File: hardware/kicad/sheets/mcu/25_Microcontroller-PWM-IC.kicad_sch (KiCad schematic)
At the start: 16 parts, among them U55 PCA9685PW,118

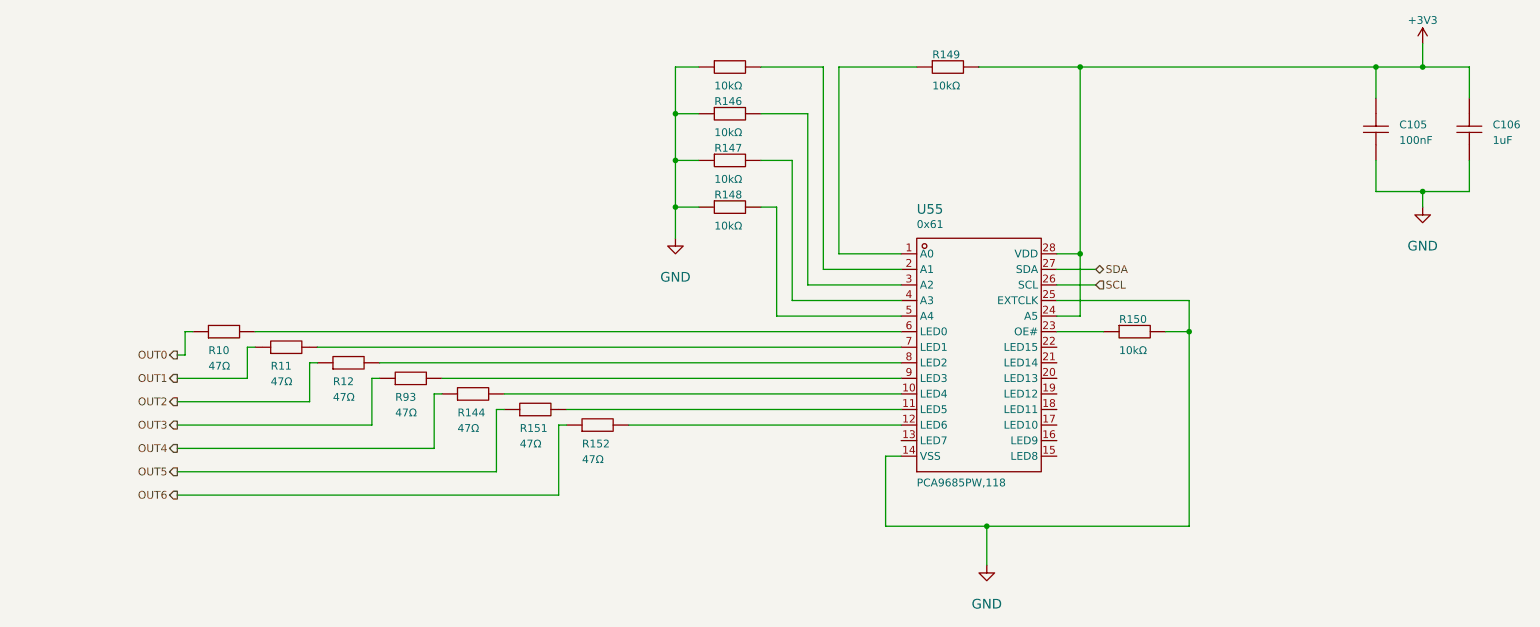
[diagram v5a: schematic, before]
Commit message: current sensing on the servos and cleaning up empty sheets
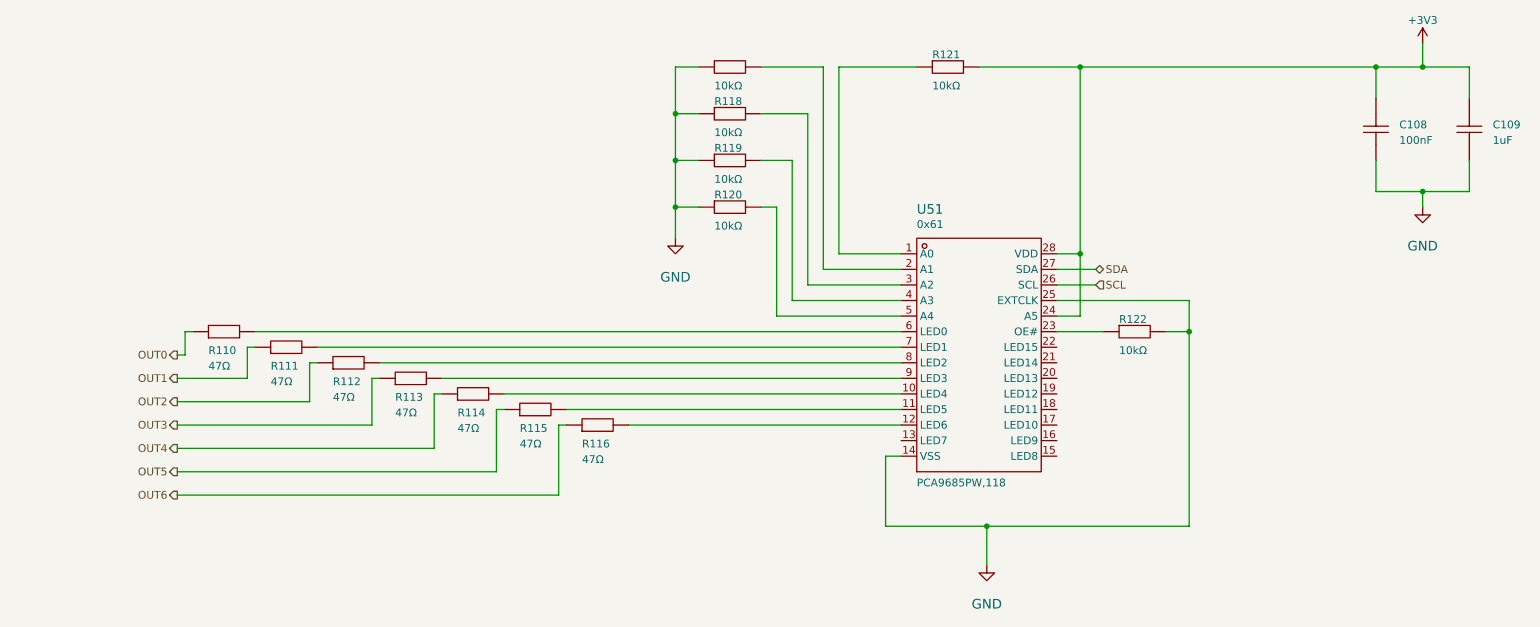
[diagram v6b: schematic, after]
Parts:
- renumbered C105 to C108, C106 to C109, R10 to R110, R11 to R111, R12 to R112, R93 to R113, R144 to R114, R151 to R115, R152 to R116, R145 to R117, R146 to R118, R147 to R119, R148 to R120, R149 to R121, R150 to R122, U55 to U51
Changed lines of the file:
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@@
 		(on_board yes)
 		(dnp no)
-		(property "Reference" "R146"
+		(property "Reference" "R118"
 			(at 128.27 71.12 0)
 			(effects
@@
 			(project "svea_powerboard_rev3"
 				(path "/3f85abf4-0b95-4c4a-b7e9-06f59ca1ea3d/5c2e021f-c2d4-49e2-8c36-9a64f1f12001/8281c4bd-f2fa-451b-b37c-f7eda375ddce"
-					(reference "R146")
+					(reference "R118")
 					(unit 1)
 				)
@@
 		(on_board yes)
 		(dnp no)
-		(property "Reference" "#PWR0175"
+		(property "Reference" "#PWR0158"
 			(at 243.84 60.96 0)
 			(effects
@@
 			(project "svea_powerboard_rev3"
 				(path "/3f85abf4-0b95-4c4a-b7e9-06f59ca1ea3d/5c2e021f-c2d4-49e2-8c36-9a64f1f12001/8281c4bd-f2fa-451b-b37c-f7eda375ddce"
-					(reference "#PWR0175")
+					(reference "#PWR0158")
 					(unit 1)
 				)
@@
 		(on_board yes)
 		(dnp no)
-		(property "Reference" "R10"
+		(property "Reference" "R110"
 			(at 45.72 111.76 0)
 			(effects
@@
 			(project "svea_powerboard_rev3"
 				(path "/3f85abf4-0b95-4c4a-b7e9-06f59ca1ea3d/5c2e021f-c2d4-49e2-8c36-9a64f1f12001/8281c4bd-f2fa-451b-b37c-f7eda375ddce"
-					(reference "R10")
+					(reference "R110")
 					(unit 1)
 				)
@@
 		(on_board yes)
 		(dnp no)
-		(property "Reference" "R144"
+		(property "Reference" "R114"
 			(at 86.36 121.92 0)
 			(effects
@@
 			(project "svea_powerboard_rev3"
 				(path "/3f85abf4-0b95-4c4a-b7e9-06f59ca1ea3d/5c2e021f-c2d4-49e2-8c36-9a64f1f12001/8281c4bd-f2fa-451b-b37c-f7eda375ddce"
-					(reference "R144")
+					(reference "R114")
 					(unit 1)
 				)
@@
 		(on_board yes)
 		(dnp no)
-		(property "Reference" "R150"
+		(property "Reference" "R122"
 			(at 194.31 106.68 0)
 			(effects
@@
 			(project "svea_powerboard_rev3"
 				(path "/3f85abf4-0b95-4c4a-b7e9-06f59ca1ea3d/5c2e021f-c2d4-49e2-8c36-9a64f1f12001/8281c4bd-f2fa-451b-b37c-f7eda375ddce"
-					(reference "R150")
+					(reference "R122")
 					(unit 1)
 				)
@@
 		(on_board yes)
 		(dnp no)
-		(property "Reference" "R11"
+		(property "Reference" "R111"
 			(at 55.88 114.3 0)
 			(effects
@@
 			(project "svea_powerboard_rev3"
 				(path "/3f85abf4-0b95-4c4a-b7e9-06f59ca1ea3d/5c2e021f-c2d4-49e2-8c36-9a64f1f12001/8281c4bd-f2fa-451b-b37c-f7eda375ddce"
-					(reference "R11")
+					(reference "R111")
 					(unit 1)
 				)
@@
 		(on_board yes)
 		(dnp no)
-		(property "Reference" "R12"
+		(property "Reference" "R112"
 			(at 66.04 116.84 0)
 			(effects
@@
 			(project "svea_powerboard_rev3"
 				(path "/3f85abf4-0b95-4c4a-b7e9-06f59ca1ea3d/5c2e021f-c2d4-49e2-8c36-9a64f1f12001/8281c4bd-f2fa-451b-b37c-f7eda375ddce"
-					(reference "R12")
+					(reference "R112")
 					(unit 1)
 				)
@@
 		(on_board yes)
 		(dnp no)
-		(property "Reference" "R93"
+		(property "Reference" "R113"
 			(at 76.2 119.38 0)
 			(effects
@@
 			(project "svea_powerboard_rev3"
 				(path "/3f85abf4-0b95-4c4a-b7e9-06f59ca1ea3d/5c2e021f-c2d4-49e2-8c36-9a64f1f12001/8281c4bd-f2fa-451b-b37c-f7eda375ddce"
-					(reference "R93")
+					(reference "R113")
 					(unit 1)
 				)
@@
 		(on_board yes)
 		(dnp no)
-		(property "Reference" "C106"
+		(property "Reference" "C109"
 			(at 255.27 74.93 90)
 			(effects
@@
 			(project "svea_powerboard_rev3"
 				(path "/3f85abf4-0b95-4c4a-b7e9-06f59ca1ea3d/5c2e021f-c2d4-49e2-8c36-9a64f1f12001/8281c4bd-f2fa-451b-b37c-f7eda375ddce"
-					(reference "C106")
+					(reference "C109")
 					(unit 1)
 				)
@@
 		(on_board yes)
 		(dnp no)
-		(property "Reference" "R149"
+		(property "Reference" "R121"
 			(at 163.83 63.5 0)
 			(effects
@@
 			(project "svea_powerboard_rev3"
 				(path "/3f85abf4-0b95-4c4a-b7e9-06f59ca1ea3d/5c2e021f-c2d4-49e2-8c36-9a64f1f12001/8281c4bd-f2fa-451b-b37c-f7eda375ddce"
-					(reference "R149")
+					(reference "R121")
 					(unit 1)
 				)
@@
 		(on_board yes)
 		(dnp no)
-		(property "Reference" "#PWR0176"
+		(property "Reference" "#PWR0159"
 			(at 243.84 87.63 0)
 			(effects
@@
 			(project "svea_powerboard_rev3"
 				(path "/3f85abf4-0b95-4c4a-b7e9-06f59ca1ea3d/5c2e021f-c2d4-49e2-8c36-9a64f1f12001/8281c4bd-f2fa-451b-b37c-f7eda375ddce"
-					(reference "#PWR0176")
+					(reference "#PWR0159")
 					(unit 1)
 				)
@@
 		(on_board yes)
 		(dnp no)
-		(property "Reference" "#PWR0173"
+		(property "Reference" "#PWR0156"
 			(at 121.92 92.71 0)
 			(effects
@@
 			(project "svea_powerboard_rev3"
 				(path "/3f85abf4-0b95-4c4a-b7e9-06f59ca1ea3d/5c2e021f-c2d4-49e2-8c36-9a64f1f12001/8281c4bd-f2fa-451b-b37c-f7eda375ddce"
-					(reference "#PWR0173")
+					(reference "#PWR0156")
 					(unit 1)
 				)
@@
 		(on_board yes)
 		(dnp no)
-		(property "Reference" "R148"
+		(property "Reference" "R120"
 			(at 128.27 86.36 0)
 			(effects
@@
 			(project "svea_powerboard_rev3"
 				(path "/3f85abf4-0b95-4c4a-b7e9-06f59ca1ea3d/5c2e021f-c2d4-49e2-8c36-9a64f1f12001/8281c4bd-f2fa-451b-b37c-f7eda375ddce"
-					(reference "R148")
+					(reference "R120")
 					(unit 1)
 				)
@@
 		(on_board yes)
 		(dnp no)
-		(property "Reference" "R145"
+		(property "Reference" "R117"
 			(at 128.27 63.5 0)
 			(effects
@@
 			(project "svea_powerboard_rev3"
 				(path "/3f85abf4-0b95-4c4a-b7e9-06f59ca1ea3d/5c2e021f-c2d4-49e2-8c36-9a64f1f12001/8281c4bd-f2fa-451b-b37c-f7eda375ddce"
-					(reference "R145")
+					(reference "R117")
 					(unit 1)
 				)
@@
 		(on_board yes)
 		(dnp no)
-		(property "Reference" "R152"
+		(property "Reference" "R116"
 			(at 106.68 127 0)
 			(effects
@@
 			(project "svea_powerboard_rev3"
 				(path "/3f85abf4-0b95-4c4a-b7e9-06f59ca1ea3d/5c2e021f-c2d4-49e2-8c36-9a64f1f12001/8281c4bd-f2fa-451b-b37c-f7eda375ddce"
-					(reference "R152")
+					(reference "R116")
 					(unit 1)
 				)
@@
 		(on_board yes)
 		(dnp no)
-		(property "Reference" "#PWR0174"
+		(property "Reference" "#PWR0157"
 			(at 172.72 146.05 0)
 			(effects
@@
 			(project "svea_powerboard_rev3"
 				(path "/3f85abf4-0b95-4c4a-b7e9-06f59ca1ea3d/5c2e021f-c2d4-49e2-8c36-9a64f1f12001/8281c4bd-f2fa-451b-b37c-f7eda375ddce"
-					(reference "#PWR0174")
+					(reference "#PWR0157")
 					(unit 1)
 				)
@@
 		(on_board yes)
 		(dnp no)
-		(property "Reference" "C105"
+		(property "Reference" "C108"
 			(at 240.03 74.93 90)
 			(effects
@@
 			(project "svea_powerboard_rev3"
 				(path "/3f85abf4-0b95-4c4a-b7e9-06f59ca1ea3d/5c2e021f-c2d4-49e2-8c36-9a64f1f12001/8281c4bd-f2fa-451b-b37c-f7eda375ddce"
-					(reference "C105")
+					(reference "C108")
 					(unit 1)
 				)
@@
 		(on_board yes)
 		(dnp no)
-		(property "Reference" "U55"
+		(property "Reference" "U51"
 			(at 161.29 88.9 0)
 			(effects
@@
 			(project "svea_powerboard_rev3"
 				(path "/3f85abf4-0b95-4c4a-b7e9-06f59ca1ea3d/5c2e021f-c2d4-49e2-8c36-9a64f1f12001/8281c4bd-f2fa-451b-b37c-f7eda375ddce"
-					(reference "U55")
+					(reference "U51")
 					(unit 1)
 				)
@@
 		(on_board yes)
 		(dnp no)
-		(property "Reference" "R147"
+		(property "Reference" "R119"
 			(at 128.27 78.74 0)
 			(effects
@@
 			(project "svea_powerboard_rev3"
 				(path "/3f85abf4-0b95-4c4a-b7e9-06f59ca1ea3d/5c2e021f-c2d4-49e2-8c36-9a64f1f12001/8281c4bd-f2fa-451b-b37c-f7eda375ddce"
-					(reference "R147")
+					(reference "R119")
 					(unit 1)
 				)
@@
 		(on_board yes)
 		(dnp no)
-		(property "Reference" "R151"
+		(property "Reference" "R115"
 			(at 96.52 124.46 0)
 			(effects
@@
 			(project "svea_powerboard_rev3"
 				(path "/3f85abf4-0b95-4c4a-b7e9-06f59ca1ea3d/5c2e021f-c2d4-49e2-8c36-9a64f1f12001/8281c4bd-f2fa-451b-b37c-f7eda375ddce"
-					(reference "R151")
+					(reference "R115")
 					(unit 1)
 				)

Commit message: new references
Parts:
- renumbered C108 to C123, C109 to C124, R110 to R146, R111 to R147, R112 to R148, R113 to R149, R114 to R150, R115 to R152, R116 to R155, R117 to R157, R118 to R158, R119 to R159, R120 to R160, R121 to R168, R122 to R171, U51 to U59
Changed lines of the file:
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@@
 		(on_board yes)
 		(dnp no)
-		(property "Reference" "R118"
+		(property "Reference" "R158"
 			(at 128.27 71.12 0)
 			(effects
@@
 			(project "svea_powerboard_rev3"
 				(path "/3f85abf4-0b95-4c4a-b7e9-06f59ca1ea3d/5c2e021f-c2d4-49e2-8c36-9a64f1f12001/8281c4bd-f2fa-451b-b37c-f7eda375ddce"
-					(reference "R118")
+					(reference "R158")
 					(unit 1)
 				)
@@
 		(on_board yes)
 		(dnp no)
-		(property "Reference" "#PWR0158"
+		(property "Reference" "#PWR0175"
 			(at 243.84 60.96 0)
 			(effects
@@
 			(project "svea_powerboard_rev3"
 				(path "/3f85abf4-0b95-4c4a-b7e9-06f59ca1ea3d/5c2e021f-c2d4-49e2-8c36-9a64f1f12001/8281c4bd-f2fa-451b-b37c-f7eda375ddce"
-					(reference "#PWR0158")
+					(reference "#PWR0175")
 					(unit 1)
 				)
@@
 		(on_board yes)
 		(dnp no)
-		(property "Reference" "R110"
+		(property "Reference" "R146"
 			(at 45.72 111.76 0)
 			(effects
@@
 			(project "svea_powerboard_rev3"
 				(path "/3f85abf4-0b95-4c4a-b7e9-06f59ca1ea3d/5c2e021f-c2d4-49e2-8c36-9a64f1f12001/8281c4bd-f2fa-451b-b37c-f7eda375ddce"
-					(reference "R110")
+					(reference "R146")
 					(unit 1)
 				)
@@
 		(on_board yes)
 		(dnp no)
-		(property "Reference" "R114"
+		(property "Reference" "R150"
 			(at 86.36 121.92 0)
 			(effects
@@
 			(project "svea_powerboard_rev3"
 				(path "/3f85abf4-0b95-4c4a-b7e9-06f59ca1ea3d/5c2e021f-c2d4-49e2-8c36-9a64f1f12001/8281c4bd-f2fa-451b-b37c-f7eda375ddce"
-					(reference "R114")
+					(reference "R150")
 					(unit 1)
 				)
@@
 		(on_board yes)
 		(dnp no)
-		(property "Reference" "R122"
+		(property "Reference" "R171"
 			(at 194.31 106.68 0)
 			(effects
@@
 			(project "svea_powerboard_rev3"
 				(path "/3f85abf4-0b95-4c4a-b7e9-06f59ca1ea3d/5c2e021f-c2d4-49e2-8c36-9a64f1f12001/8281c4bd-f2fa-451b-b37c-f7eda375ddce"
-					(reference "R122")
+					(reference "R171")
 					(unit 1)
 				)
@@
 		(on_board yes)
 		(dnp no)
-		(property "Reference" "R111"
+		(property "Reference" "R147"
 			(at 55.88 114.3 0)
 			(effects
@@
 			(project "svea_powerboard_rev3"
 				(path "/3f85abf4-0b95-4c4a-b7e9-06f59ca1ea3d/5c2e021f-c2d4-49e2-8c36-9a64f1f12001/8281c4bd-f2fa-451b-b37c-f7eda375ddce"
-					(reference "R111")
+					(reference "R147")
 					(unit 1)
 				)
@@
 		(on_board yes)
 		(dnp no)
-		(property "Reference" "R112"
+		(property "Reference" "R148"
 			(at 66.04 116.84 0)
 			(effects
@@
 			(project "svea_powerboard_rev3"
 				(path "/3f85abf4-0b95-4c4a-b7e9-06f59ca1ea3d/5c2e021f-c2d4-49e2-8c36-9a64f1f12001/8281c4bd-f2fa-451b-b37c-f7eda375ddce"
-					(reference "R112")
+					(reference "R148")
 					(unit 1)
 				)
@@
 		(on_board yes)
 		(dnp no)
-		(property "Reference" "R113"
+		(property "Reference" "R149"
 			(at 76.2 119.38 0)
 			(effects
@@
 			(project "svea_powerboard_rev3"
 				(path "/3f85abf4-0b95-4c4a-b7e9-06f59ca1ea3d/5c2e021f-c2d4-49e2-8c36-9a64f1f12001/8281c4bd-f2fa-451b-b37c-f7eda375ddce"
-					(reference "R113")
+					(reference "R149")
 					(unit 1)
 				)
@@
 		(on_board yes)
 		(dnp no)
-		(property "Reference" "C109"
+		(property "Reference" "C124"
 			(at 255.27 74.93 90)
 			(effects
@@
 			(project "svea_powerboard_rev3"
 				(path "/3f85abf4-0b95-4c4a-b7e9-06f59ca1ea3d/5c2e021f-c2d4-49e2-8c36-9a64f1f12001/8281c4bd-f2fa-451b-b37c-f7eda375ddce"
-					(reference "C109")
+					(reference "C124")
 					(unit 1)
 				)
@@
 		(on_board yes)
 		(dnp no)
-		(property "Reference" "R121"
+		(property "Reference" "R168"
 			(at 163.83 63.5 0)
 			(effects
@@
 			(project "svea_powerboard_rev3"
 				(path "/3f85abf4-0b95-4c4a-b7e9-06f59ca1ea3d/5c2e021f-c2d4-49e2-8c36-9a64f1f12001/8281c4bd-f2fa-451b-b37c-f7eda375ddce"
-					(reference "R121")
+					(reference "R168")
 					(unit 1)
 				)
@@
 		(on_board yes)
 		(dnp no)
-		(property "Reference" "#PWR0159"
+		(property "Reference" "#PWR0176"
 			(at 243.84 87.63 0)
 			(effects
@@
 			(project "svea_powerboard_rev3"
 				(path "/3f85abf4-0b95-4c4a-b7e9-06f59ca1ea3d/5c2e021f-c2d4-49e2-8c36-9a64f1f12001/8281c4bd-f2fa-451b-b37c-f7eda375ddce"
-					(reference "#PWR0159")
+					(reference "#PWR0176")
 					(unit 1)
 				)
@@
 		(on_board yes)
 		(dnp no)
-		(property "Reference" "#PWR0156"
+		(property "Reference" "#PWR0173"
 			(at 121.92 92.71 0)
 			(effects
@@
 			(project "svea_powerboard_rev3"
 				(path "/3f85abf4-0b95-4c4a-b7e9-06f59ca1ea3d/5c2e021f-c2d4-49e2-8c36-9a64f1f12001/8281c4bd-f2fa-451b-b37c-f7eda375ddce"
-					(reference "#PWR0156")
+					(reference "#PWR0173")
 					(unit 1)
 				)
@@
 		(on_board yes)
 		(dnp no)
-		(property "Reference" "R120"
+		(property "Reference" "R160"
 			(at 128.27 86.36 0)
 			(effects
@@
 			(project "svea_powerboard_rev3"
 				(path "/3f85abf4-0b95-4c4a-b7e9-06f59ca1ea3d/5c2e021f-c2d4-49e2-8c36-9a64f1f12001/8281c4bd-f2fa-451b-b37c-f7eda375ddce"
-					(reference "R120")
+					(reference "R160")
 					(unit 1)
 				)
@@
 		(on_board yes)
 		(dnp no)
-		(property "Reference" "R117"
+		(property "Reference" "R157"
 			(at 128.27 63.5 0)
 			(effects
@@
 			(project "svea_powerboard_rev3"
 				(path "/3f85abf4-0b95-4c4a-b7e9-06f59ca1ea3d/5c2e021f-c2d4-49e2-8c36-9a64f1f12001/8281c4bd-f2fa-451b-b37c-f7eda375ddce"
-					(reference "R117")
+					(reference "R157")
 					(unit 1)
 				)
@@
 		(on_board yes)
 		(dnp no)
-		(property "Reference" "R116"
+		(property "Reference" "R155"
 			(at 106.68 127 0)
 			(effects
@@
 			(project "svea_powerboard_rev3"
 				(path "/3f85abf4-0b95-4c4a-b7e9-06f59ca1ea3d/5c2e021f-c2d4-49e2-8c36-9a64f1f12001/8281c4bd-f2fa-451b-b37c-f7eda375ddce"
-					(reference "R116")
+					(reference "R155")
 					(unit 1)
 				)
@@
 		(on_board yes)
 		(dnp no)
-		(property "Reference" "#PWR0157"
+		(property "Reference" "#PWR0174"
 			(at 172.72 146.05 0)
 			(effects
@@
 			(project "svea_powerboard_rev3"
 				(path "/3f85abf4-0b95-4c4a-b7e9-06f59ca1ea3d/5c2e021f-c2d4-49e2-8c36-9a64f1f12001/8281c4bd-f2fa-451b-b37c-f7eda375ddce"
-					(reference "#PWR0157")
+					(reference "#PWR0174")
 					(unit 1)
 				)
@@
 		(on_board yes)
 		(dnp no)
-		(property "Reference" "C108"
+		(property "Reference" "C123"
 			(at 240.03 74.93 90)
 			(effects
@@
 			(project "svea_powerboard_rev3"
 				(path "/3f85abf4-0b95-4c4a-b7e9-06f59ca1ea3d/5c2e021f-c2d4-49e2-8c36-9a64f1f12001/8281c4bd-f2fa-451b-b37c-f7eda375ddce"
-					(reference "C108")
+					(reference "C123")
 					(unit 1)
 				)
@@
 		(on_board yes)
 		(dnp no)
-		(property "Reference" "U51"
+		(property "Reference" "U59"
 			(at 161.29 88.9 0)
 			(effects
@@
 			(project "svea_powerboard_rev3"
 				(path "/3f85abf4-0b95-4c4a-b7e9-06f59ca1ea3d/5c2e021f-c2d4-49e2-8c36-9a64f1f12001/8281c4bd-f2fa-451b-b37c-f7eda375ddce"
-					(reference "U51")
+					(reference "U59")
 					(unit 1)
 				)
@@
 		(on_board yes)
 		(dnp no)
-		(property "Reference" "R119"
+		(property "Reference" "R159"
 			(at 128.27 78.74 0)
 			(effects
@@
 			(project "svea_powerboard_rev3"
 				(path "/3f85abf4-0b95-4c4a-b7e9-06f59ca1ea3d/5c2e021f-c2d4-49e2-8c36-9a64f1f12001/8281c4bd-f2fa-451b-b37c-f7eda375ddce"
-					(reference "R119")
+					(reference "R159")
 					(unit 1)
 				)
@@
 		(on_board yes)
 		(dnp no)
-		(property "Reference" "R115"
+		(property "Reference" "R152"
 			(at 96.52 124.46 0)
 			(effects
@@
 			(project "svea_powerboard_rev3"
 				(path "/3f85abf4-0b95-4c4a-b7e9-06f59ca1ea3d/5c2e021f-c2d4-49e2-8c36-9a64f1f12001/8281c4bd-f2fa-451b-b37c-f7eda375ddce"
-					(reference "R115")
+					(reference "R152")
 					(unit 1)
 				)
